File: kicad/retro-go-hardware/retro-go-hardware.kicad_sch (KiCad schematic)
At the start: 27 parts, among them SW1 ON / OFF Switch

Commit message: Added battery level probe
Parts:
- added R5, R6: 100K, symbol Device:R_Small
- R1, R2, R3, R4: value 100K -> 33K
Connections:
- net at MT3608-Module1. (Vout), SW1.2 (B): now also R6.1
- net at ILI9341. (RES): no longer ESP32-S3-DevKitC-1. (RST)
- new net: DAC-I2S-MAX98357A. (Vin-3V-6V), ESP32-S3-DevKitC-1. (RST) (x3)
- new net: ESP32-S3-DevKitC-1. (RST), SD-Card-SPI-Module. (MOSI) (x4)
- new net: MT3608-Module1. (Vout), R5.2, TP4056-DW01A-Module1. (Vout)
- new net: ESP32-S3-DevKitC-1. (RST), ILI9341. (RES) (x5)
- new net Battery level: ESP32-S3-DevKitC-1. (RST)
- new net Battery level GPIO04: R5.1, R6.2
- now unconnected: ILI9341. (RES), ILI9341. (RES), ILI9341. (RES), ILI9341. (RES)
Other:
- moved on the sheet: 100n, 100n1, 2.7uF, 2.7uF1, BT1, BUTTON-A, BUTTON-B, DAC-I2S-MAX98357A, ESP32-S3-DevKitC-1, ILI9341, MENU, MT3608-Module1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

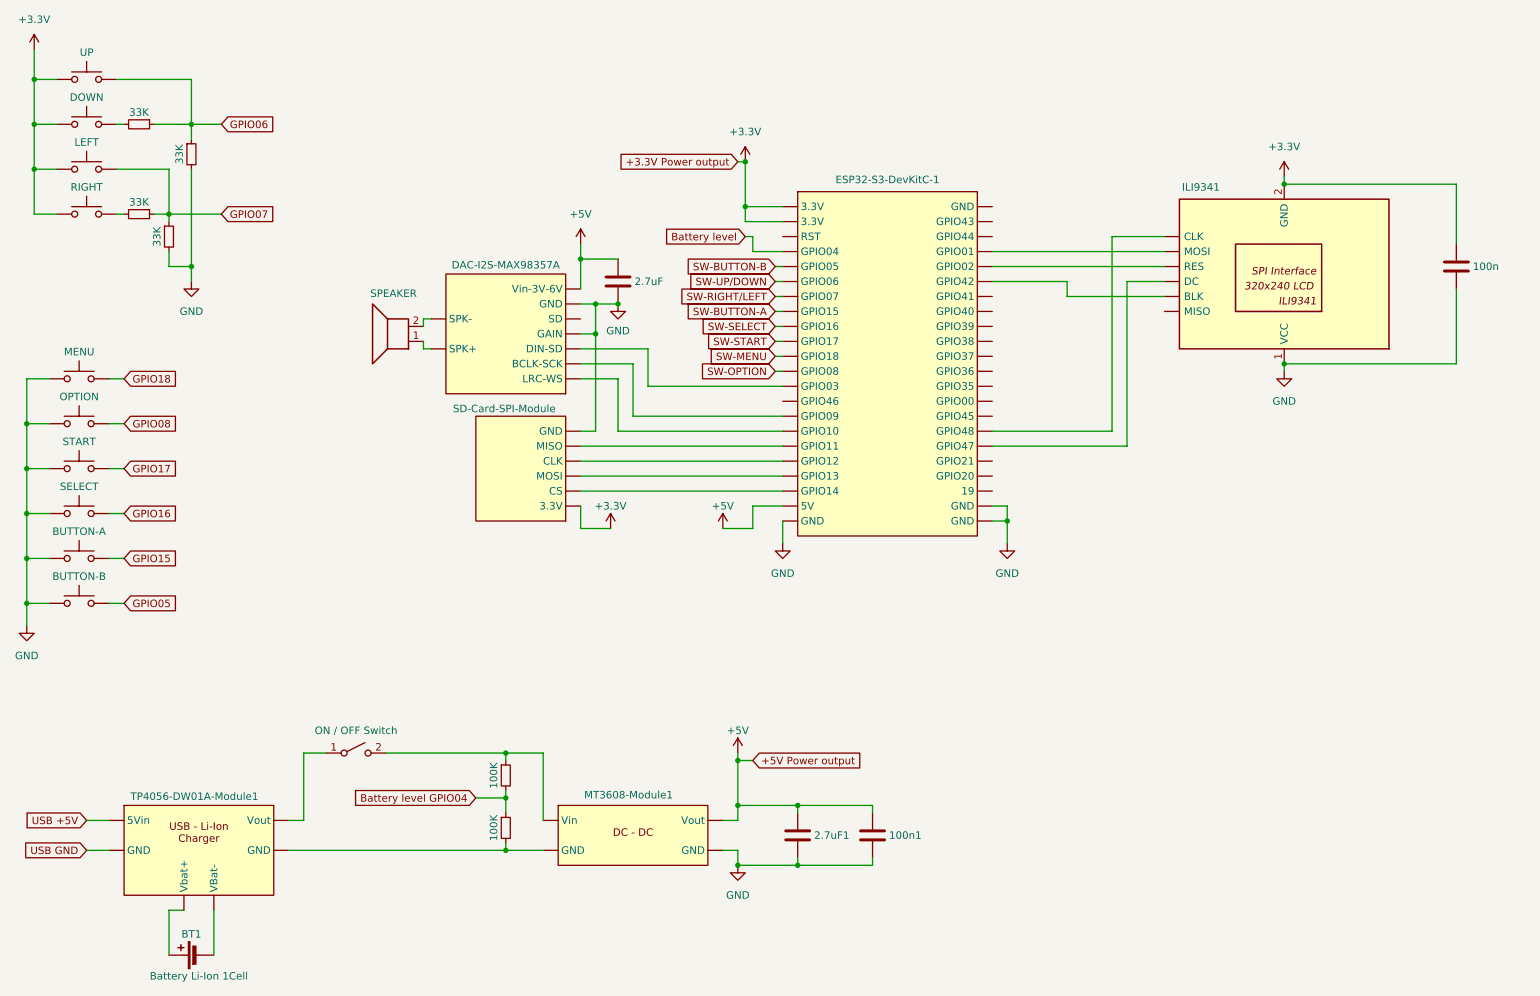
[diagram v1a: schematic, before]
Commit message: Added antinoise capacitors
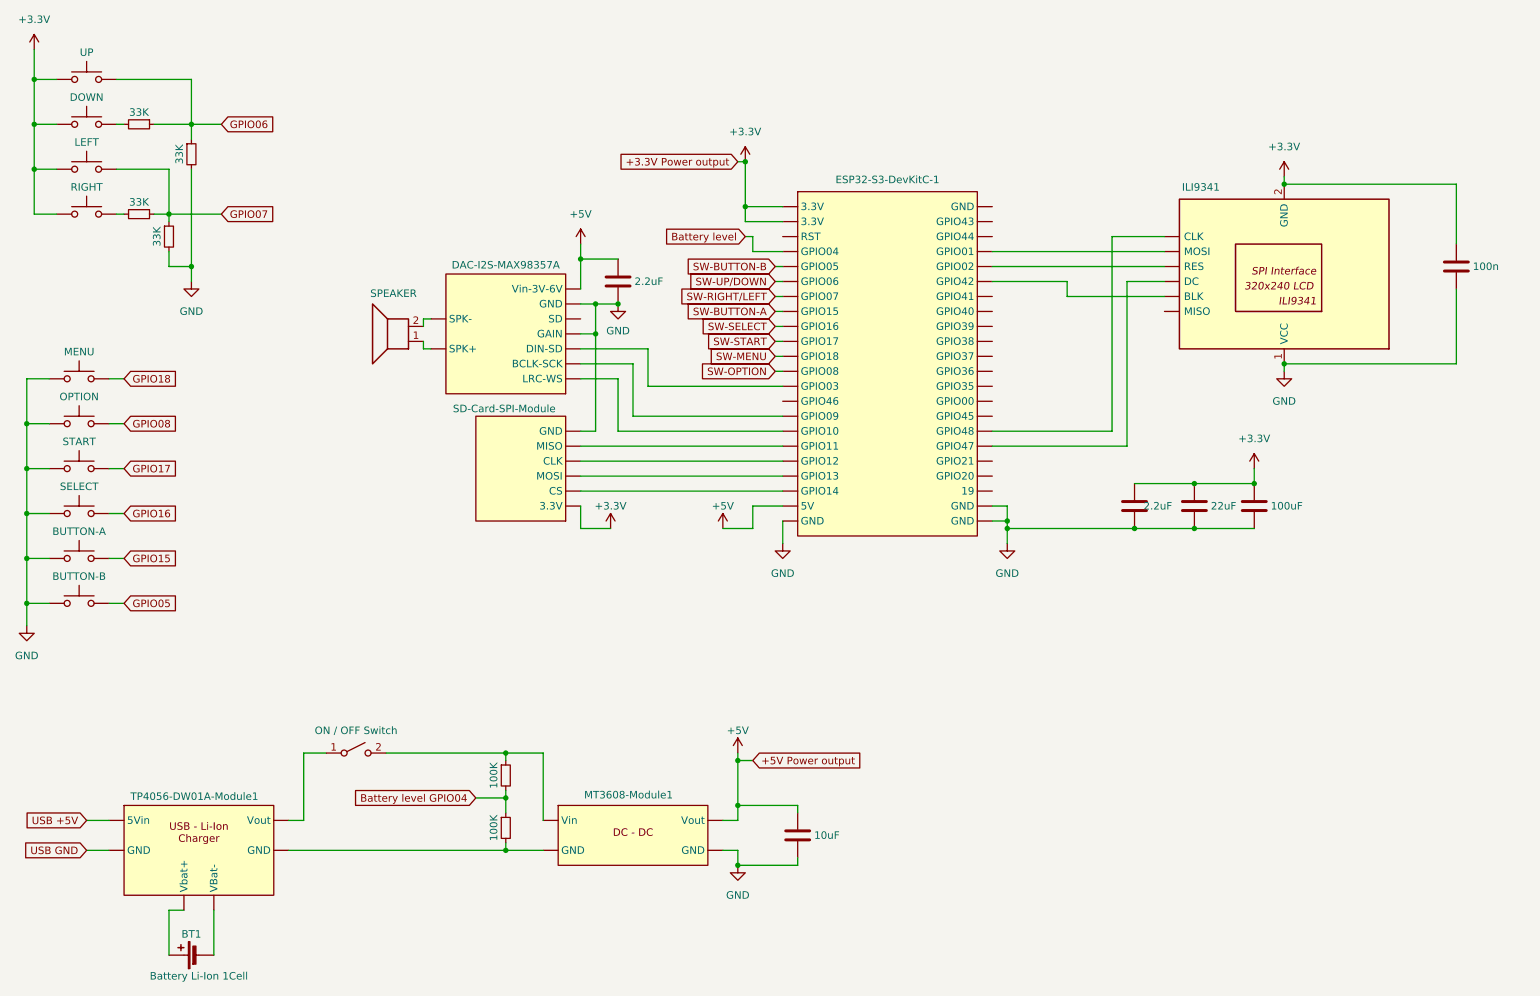
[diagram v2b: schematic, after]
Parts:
- removed 100n1: C, symbol Device:C
- added 100uF, 2.2uF, 22uF: C, symbol Device:C
- renumbered 2.7uF1 to 10uF, 2.7uF to 2.2uF
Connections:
- net +3.3V: now also 100uF.1, 2.2uF.1, 22uF.1
- net GND: now also 100uF.2, 2.2uF.2, 22uF.2
- net at ILI9341. (RES): no longer ESP32-S3-DevKitC-1. (RST)
- new net: DAC-I2S-MAX98357A. (Vin-3V-6V), ESP32-S3-DevKitC-1. (RST) (x3)
- new net: ESP32-S3-DevKitC-1. (RST), SD-Card-SPI-Module. (MOSI) (x4)
- new net: MT3608-Module1. (Vout), R5.2, TP4056-DW01A-Module1. (Vout)
- new net: ESP32-S3-DevKitC-1. (RST), ILI9341. (RES) (x5)
- now unconnected: ILI9341. (RES), ILI9341. (RES), ILI9341. (RES), ILI9341. (RES)

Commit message: Realigned schematic
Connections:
- net at ILI9341. (RES): no longer ESP32-S3-DevKitC-1. (RST)
- new net: DAC-I2S-MAX98357A. (Vin-3V-6V), ESP32-S3-DevKitC-1. (RST) (x3)
- new net: ESP32-S3-DevKitC-1. (RST), SD-Card-SPI-Module. (MOSI) (x4)
- new net: MT3608-Module1. (Vout), R5.2, TP4056-DW01A-Module1. (Vout)
- new net: ESP32-S3-DevKitC-1. (RST), ILI9341. (RES) (x5)
- now unconnected: ILI9341. (RES), ILI9341. (RES), ILI9341. (RES), ILI9341. (RES)
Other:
- moved on the sheet: 100uF, 2.2uF, 22uF
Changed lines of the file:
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@@
 	)
 	(junction
-		(at 186.69 110.49)
-		(diameter 0)
-		(color 0 0 0 0)
-	)
-	(junction
-		(at 228.6 102.87)
+		(at 228.6 101.6)
 		(diameter 0)
 		(color 0 0 0 0)
@@
 	)
 	(junction
-		(at 218.44 110.49)
+		(at 218.44 109.22)
 		(diameter 0)
 		(color 0 0 0 0)
@@
 	)
 	(junction
-		(at 218.44 102.87)
+		(at 218.44 101.6)
 		(diameter 0)
 		(color 0 0 0 0)
@@
 	)
 	(junction
-		(at 208.28 110.49)
+		(at 208.28 109.22)
 		(diameter 0)
 		(color 0 0 0 0)
@@
 	(wire
 		(pts
-			(xy 186.69 109.22) (xy 186.69 110.49)
-		)
-		(stroke
-			(width 0)
-			(type default)
-		)
-	)
-	(wire
-		(pts
 			(xy 20.32 115.57) (xy 20.32 123.19)
 		)
@@
 	(wire
 		(pts
-			(xy 208.28 102.87) (xy 218.44 102.87)
+			(xy 208.28 101.6) (xy 218.44 101.6)
 		)
 		(stroke
@@
 	(wire
 		(pts
-			(xy 208.28 110.49) (xy 218.44 110.49)
+			(xy 208.28 109.22) (xy 218.44 109.22)
 		)
 		(stroke
@@
 	(wire
 		(pts
-			(xy 228.6 102.87) (xy 228.6 100.33)
+			(xy 228.6 101.6) (xy 228.6 99.06)
 		)
 		(stroke
@@
 	(wire
 		(pts
-			(xy 186.69 110.49) (xy 186.69 113.03)
+			(xy 186.69 109.22) (xy 186.69 113.03)
 		)
 		(stroke
@@
 	(wire
 		(pts
-			(xy 218.44 110.49) (xy 228.6 110.49)
+			(xy 218.44 109.22) (xy 228.6 109.22)
 		)
 		(stroke
@@
 	(wire
 		(pts
-			(xy 186.69 110.49) (xy 208.28 110.49)
+			(xy 186.69 109.22) (xy 208.28 109.22)
 		)
 		(stroke
@@
 	(wire
 		(pts
-			(xy 218.44 102.87) (xy 228.6 102.87)
+			(xy 218.44 101.6) (xy 228.6 101.6)
 		)
 		(stroke
@@
 	(symbol
 		(lib_id "power:+3.3V")
-		(at 228.6 100.33 0)
+		(at 228.6 99.06 0)
 		(unit 1)
 		(exclude_from_sim no)
@@
 		(fields_autoplaced yes)
 		(property "Reference" "#PWR015"
-			(at 228.6 104.14 0)
+			(at 228.6 102.87 0)
 			(effects
 				(font
@@
 		)
 		(property "Value" "+3.3V"
-			(at 228.6 95.25 0)
+			(at 228.6 93.98 0)
 			(effects
 				(font
@@
 		)
 		(property "Footprint" ""
-			(at 228.6 100.33 0)
+			(at 228.6 99.06 0)
 			(effects
 				(font
@@
 		)
 		(property "Datasheet" ""
-			(at 228.6 100.33 0)
+			(at 228.6 99.06 0)
 			(effects
 				(font
@@
 		)
 		(property "Description" "Power symbol creates a global label with name \"+3.3V\""
-			(at 228.6 100.33 0)
+			(at 228.6 99.06 0)
 			(effects
 				(font
@@
 	(symbol
 		(lib_id "Device:C")
-		(at 228.6 106.68 0)
+		(at 228.6 105.41 0)
 		(unit 1)
 		(exclude_from_sim no)
@@
 		(dnp no)
 		(property "Reference" "100uF"
-			(at 231.394 106.68 0)
+			(at 231.394 105.41 0)
 			(effects
 				(font
@@
 		)
 		(property "Value" "C"
-			(at 232.41 107.9499 0)
+			(at 232.41 106.6799 0)
 			(effects
 				(font
@@
 		)
 		(property "Footprint" ""
-			(at 229.5652 110.49 0)
+			(at 229.5652 109.22 0)
 			(effects
 				(font
@@
 		)
 		(property "Datasheet" "~"
-			(at 228.6 106.68 0)
+			(at 228.6 105.41 0)
 			(effects
 				(font
@@
 		)
 		(property "Description" "Unpolarized capacitor"
-			(at 228.6 106.68 0)
+			(at 228.6 105.41 0)
 			(effects
 				(font
@@
 	(symbol
 		(lib_id "Device:C")
-		(at 208.28 106.68 0)
+		(at 208.28 105.41 0)
 		(unit 1)
 		(exclude_from_sim no)
@@
 		(dnp no)
 		(property "Reference" "2.2uF"
-			(at 209.804 106.68 0)
+			(at 210.566 105.41 0)
 			(effects
 				(font
@@
 		)
 		(property "Value" "C"
-			(at 212.09 107.9499 0)
+			(at 212.09 106.6799 0)
 			(effects
 				(font
@@
 		)
 		(property "Footprint" ""
-			(at 209.2452 110.49 0)
+			(at 209.2452 109.22 0)
 			(effects
 				(font
@@
 		)
 		(property "Datasheet" "~"
-			(at 208.28 106.68 0)
+			(at 208.28 105.41 0)
 			(effects
 				(font
@@
 		)
 		(property "Description" "Unpolarized capacitor"
-			(at 208.28 106.68 0)
+			(at 208.28 105.41 0)
 			(effects
 				(font
@@
 	(symbol
 		(lib_id "Device:C")
-		(at 218.44 106.68 0)
+		(at 218.44 105.41 0)
 		(unit 1)
 		(exclude_from_sim no)
@@
 		(dnp no)
 		(property "Reference" "22uF"
-			(at 221.234 106.68 0)
+			(at 221.234 105.41 0)
 			(effects
 				(font
@@
 		)
 		(property "Value" "C"
-			(at 222.25 107.9499 0)
+			(at 222.25 106.6799 0)
 			(effects
 				(font
@@
 		)
 		(property "Footprint" ""
-			(at 219.4052 110.49 0)
+			(at 219.4052 109.22 0)
 			(effects
 				(font
@@
 		)
 		(property "Datasheet" "~"
-			(at 218.44 106.68 0)
+			(at 218.44 105.41 0)
 			(effects
 				(font
@@
 		)
 		(property "Description" "Unpolarized capacitor"
-			(at 218.44 106.68 0)
+			(at 218.44 105.41 0)
 			(effects
 				(font
